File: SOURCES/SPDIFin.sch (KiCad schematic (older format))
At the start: 0 parts

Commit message: test dev
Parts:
- added J?: AUDIO_JACK_STEREO_12PIN_FCR1117, symbol AUDIO_JACK_STEREO_12PIN_FCR1117
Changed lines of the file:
@@
 Comment4 ""
 $EndDescr
+$Comp
+L AUDIO_JACK_STEREO_12PIN_FCR1117 J?
+U 1 1 5AFAD10C
+P 4800 3000
+F 0 "J?" H 4800 2300 50  0000 C CNN
+F 1 "AUDIO_JACK_STEREO_12PIN_FCR1117" H 4800 3800 50  0000 C CNN
+F 2 "" H 5050 3500 60  0000 C CNN
+F 3 "" H 5050 3500 60  0000 C CNN
+	1    4800 3000
+	1    0    0    -1
+$EndComp
 $EndSCHEMATC

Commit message: test
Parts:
- added P?: CONN_01X01, symbol CONN_01X01
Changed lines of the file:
@@
+	1    0    0    -1
+$EndComp
+$Comp
+L CONN_01X01 P?
+U 1 1 5AFC267D
+P 7550 2750
+F 0 "P?" H 7550 2850 50  0000 C CNN
+F 1 "CONN_01X01" V 7650 2750 50  0000 C CNN
+F 2 "" H 7550 2750 60  0000 C CNN
+F 3 "" H 7550 2750 60  0000 C CNN
+	1    7550 2750
 	1    0    0    -1
 $EndComp

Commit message: added SPDIF lib & analog out
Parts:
- removed J?: AUDIO_JACK_STEREO_12PIN_FCR1117, symbol AUDIO_JACK_STEREO_12PIN_FCR1117
- removed P?: CONN_01X01, symbol CONN_01X01
- added U?: CS8422-CNZ, CIR-QFN-32_5X5, symbol CS8422-CNZ
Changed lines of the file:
@@
 LIBS:Polarized_Cap
 LIBS:tas5760mdcar
+LIBS:symbols-CS8422-CNZ
+LIBS:symbols_CS8406-CZZ
 LIBS:smd_aio-cache
 EELAYER 25 0
@@
 $EndDescr
 $Comp
-L AUDIO_JACK_STEREO_12PIN_FCR1117 J?
-U 1 1 5AFAD10C
-P 4800 3000
-F 0 "J?" H 4800 2300 50  0000 C CNN
-F 1 "AUDIO_JACK_STEREO_12PIN_FCR1117" H 4800 3800 50  0000 C CNN
-F 2 "" H 5050 3500 60  0000 C CNN
-F 3 "" H 5050 3500 60  0000 C CNN
-	1    4800 3000
+L CS8422-CNZ U?
+U 1 1 5B04A0D3
+P 4290 3150
+F 0 "U?" H 5790 3550 60  0000 C CNN
+F 1 "CS8422-CNZ" H 5790 3450 60  0000 C CNN
+F 2 "CIR-QFN-32_5X5" H 5790 3390 60  0001 C CNN
+F 3 "" H 4290 3150 60  0000 C CNN
+	1    4290 3150
 	1    0    0    -1
 $EndComp
-$Comp
-L CONN_01X01 P?
-U 1 1 5AFC267D
-P 7550 2750
-F 0 "P?" H 7550 2850 50  0000 C CNN
-F 1 "CONN_01X01" V 7650 2750 50  0000 C CNN
-F 2 "" H 7550 2750 60  0000 C CNN
-F 3 "" H 7550 2750 60  0000 C CNN
-	1    7550 2750
-	1    0    0    -1
-$EndComp

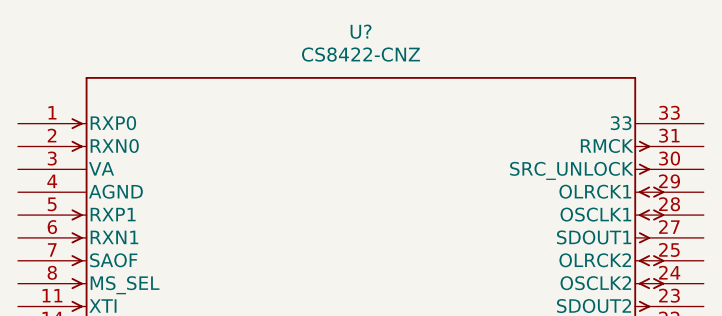
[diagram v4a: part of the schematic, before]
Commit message: added analog input
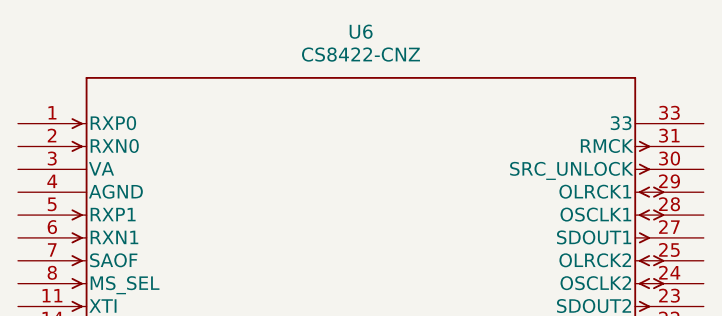
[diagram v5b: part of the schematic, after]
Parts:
- gave numbers to parts that had none: 1
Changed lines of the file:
@@
 $EndDescr
 $Comp
-L CS8422-CNZ U?
+L CS8422-CNZ U6
 U 1 1 5B04A0D3
 P 4290 3150
-F 0 "U?" H 5790 3550 60  0000 C CNN
+F 0 "U6" H 5790 3550 60  0000 C CNN
 F 1 "CS8422-CNZ" H 5790 3450 60  0000 C CNN
 F 2 "CIR-QFN-32_5X5" H 5790 3390 60  0001 C CNN

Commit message: Spdif Schaltpläne
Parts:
- added C72: 10n, symbol C
- added C? (x4): 100n, symbol C
- added C? (x3): 10µ, symbol CP
- added D? (x2): LED, symbol LED
- added R? (x2): 1k, symbol R
- added R? (x2): 20k, symbol R
- added R?: 32k4, symbol R
- added R?: 16k2, symbol R
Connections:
- net labels added: +3V3, BRD_RST, GND, MCLK4, MP0, MP4, MP5, SPDIF_In
- wire segments 0 -> 51
- no-connect marks 0 -> 11
